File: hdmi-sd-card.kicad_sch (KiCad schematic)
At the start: 76 parts, among them J11 I-PEX_CABLINE-VS_1x20_20455-A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, J4 HDMI-A_WE_685119134923, J5 MicroSD_693071020811, U10 TPD4E05U06QDQARQ1, U11 TPD4E05U06QDQARQ1, U12 TPD4E05U06QDQARQ1, U14 TPD4E05U06QDQARQ1, U37 TPD4E05U06QDQARQ1, U38 SN65DP159RGZR, U40 NVT4858_XQFN, U41 TPD4E05U06QDQARQ1, U43 TPS2116DRLR

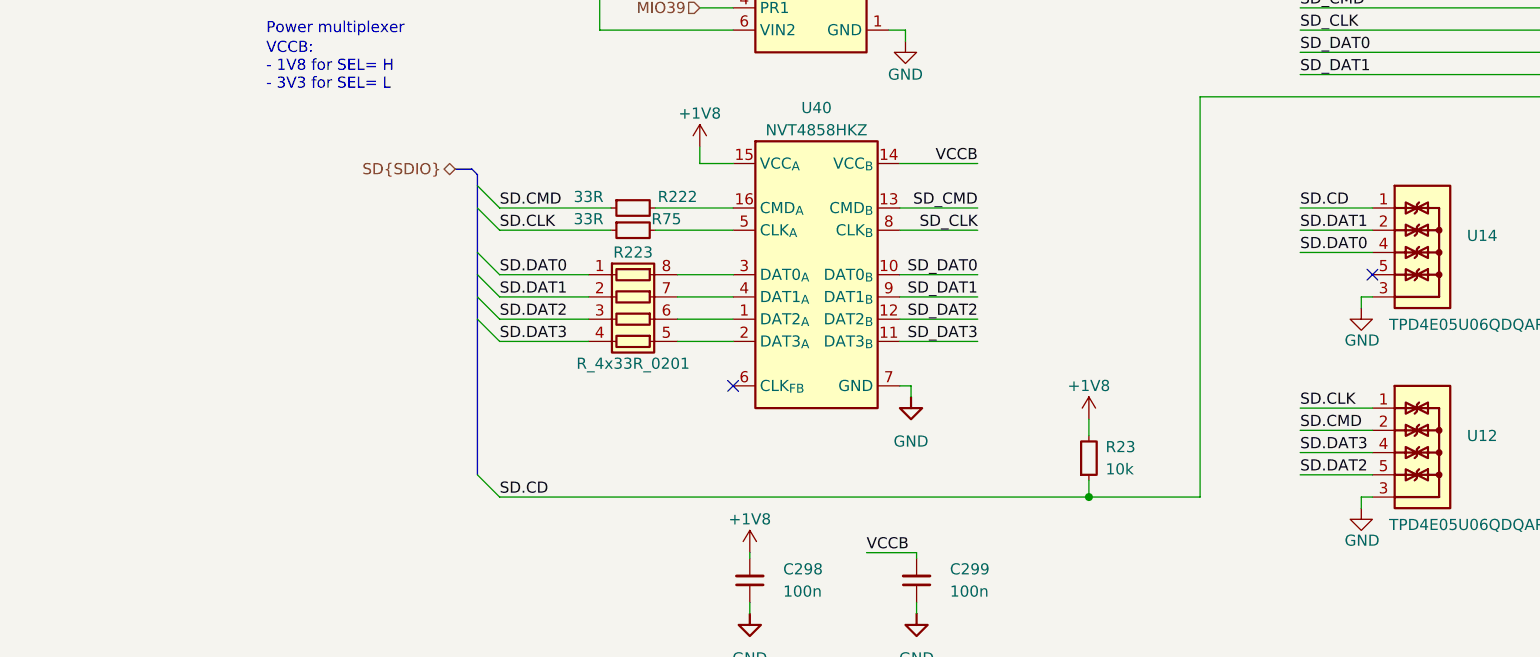
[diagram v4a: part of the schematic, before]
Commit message: [#67016] Connect SD card
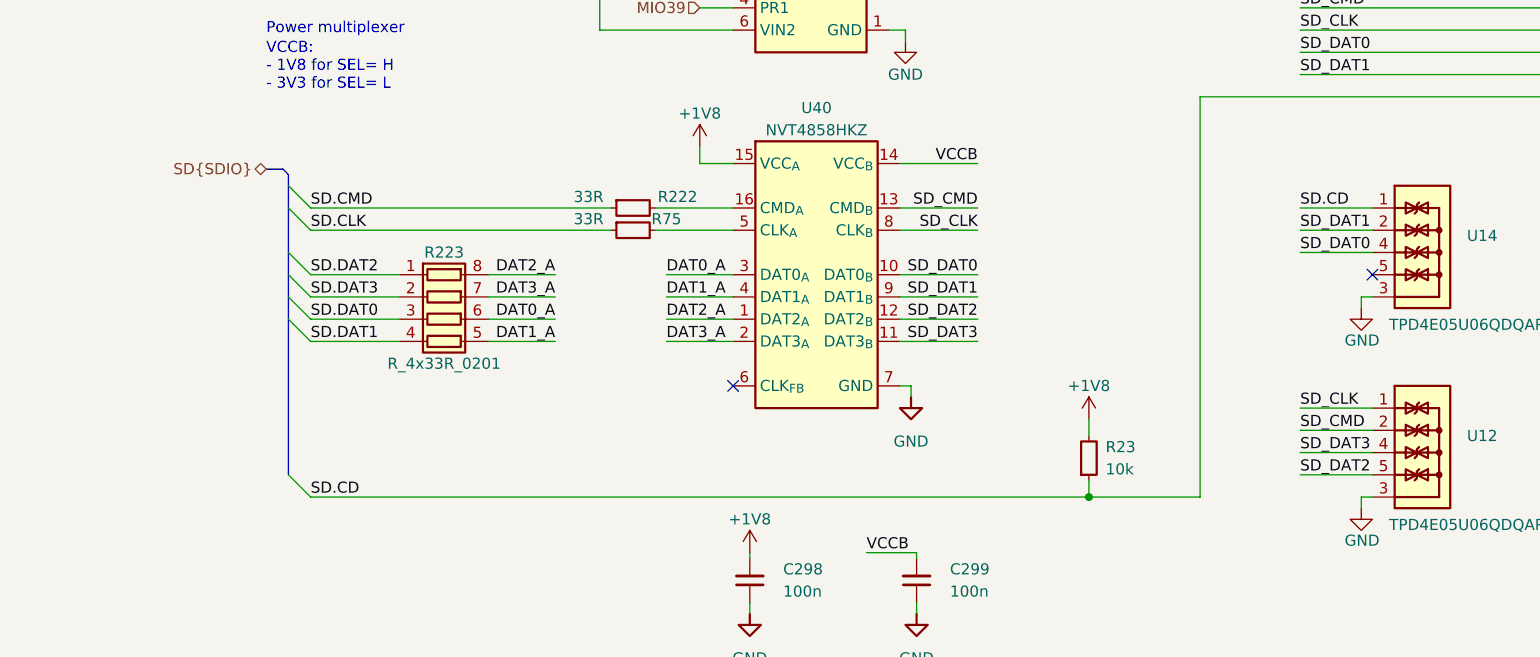
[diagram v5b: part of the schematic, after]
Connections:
- net SD.CLK: no longer U12.1, U12.10
- net SD.CMD: no longer U12.2, U12.9
- net SD.DAT0: now also R223.3 (R3.1); no longer R223.1 (R1.1), U14.4, U14.7
- net SD.DAT1: now also R223.4 (R4.1); no longer R223.2 (R2.1), U14.2, U14.9
- net SD.DAT2: now also R223.1 (R1.1); no longer R223.3 (R3.1), U12.5, U12.6
- net SD.DAT3: now also R223.2 (R2.1); no longer R223.4 (R4.1), U12.4, U12.7
- net SD_CLK: now also U12.1, U12.10
- net SD_CMD: now also U12.2, U12.9
- net SD_DAT0: now also U14.4, U14.7
- net SD_DAT1: now also U14.2, U14.9
- net SD_DAT2: now also U12.5, U12.6
- net SD_DAT3: now also U12.4, U12.7
- net DAT0_A: now reaches R223.6 (R3.2)
- net DAT0_A: now also U40.3 (DAT0_{A}); no longer U40.1 (DAT2_{A})
- net DAT1_A: now reaches R223.5 (R4.2)
- net DAT1_A: now also U40.4 (DAT1_{A}); no longer U40.2 (DAT3_{A})
- net DAT2_A: now reaches R223.8 (R1.2)
- net DAT2_A: now also U40.1 (DAT2_{A}); no longer U40.3 (DAT0_{A})
- net DAT3_A: now reaches R223.7 (R2.2)
- net DAT3_A: now also U40.2 (DAT3_{A}); no longer U40.4 (DAT1_{A})
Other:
- moved on the sheet: R223

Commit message: [#66312] Continued HDMI schematic connections
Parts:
- added C29, C82, C93: C_100n_0402, antmicro-footprints:C_0402_1005Metric, symbol antmicroCapacitors0402:C_100n_0402
- added Q18, Q19, Q21: BSS138PW, antmicro-footprints:SC70-3, symbol antmicroTransistorsFETsMOSFETsSingle:BSS138PW
- added R38: R_0R_0402, antmicro-footprints:R_0402_1005Metric, symbol antmicroResistors0402:R_0R_0402
- added R81, R82: R_1k_0402, antmicro-footprints:R_0402_1005Metric, symbol antmicroResistors0402:R_1k_0402
- added R83: R_100k_0402, antmicro-footprints:R_0402_1005Metric, symbol antmicroResistors0402:R_100k_0402
- added R85, R86: R_10k_0402, antmicro-footprints:R_0402_1005Metric, symbol antmicroResistors0402:R_10k_0402
- added U42: M24C64-F_DFN8, antmicro-footprints:DFN-8-1EP_3x2mm_P0.5mm_EP1.36x1.46mm, symbol antmicroMemory:M24C64-F_DFN8
- added U44: TXS0102DQER, antmicro-footprints:X2SON8_1.4x1x0.32mm_P0.35mm, symbol antmicroLogicTranslatorsLevelShifters:TXS0102DQER
- added U47, U48: TPD4E05U06QDQARQ1, antmicro-footprints:USON-10_2.5x1mm_P0.5mm, symbol antmicroTVSDiodes:TPD4E05U06QDQARQ1
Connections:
- net HDMI_HOTPLUG is gone; now on net I2C_EN/PIN: U38.10 (I2C_EN/PIN)
- net HDMI_IN_CONN_CLK_N is gone; now on net HDMI_IN.CLK_N: U41.5, U41.6
- net HDMI_IN_CONN_CLK_P is gone; now on net HDMI_IN.CLK_P: U41.4, U41.7
- net HDMI_IN_CONN_D0_N is gone; now on net HDMI_IN.D0_N: U41.2, U41.9
- net HDMI_IN_CONN_D0_P is gone; now on net HDMI_IN.D0_P: U41.1, U41.10
- net HDMI_IN_CONN_D1_N is gone; now on net HDMI_IN.D1_N: U37.5, U37.6
- net HDMI_IN_CONN_D1_P is gone; now on net HDMI_IN.D1_P: U37.4, U37.7
- net HDMI_IN_CONN_D2_N is gone; now on net HDMI_IN.D2_N: U37.2, U37.9
- net HDMI_IN_CONN_D2_P is gone; now on net HDMI_IN.D2_P: U37.1, U37.10
- net +3V3: now also C29.1, C82.1, R86.2, U42.8 (VCC), U44.1 (VCCA), U44.5 (OE)
- net +5V: no longer R72.2, R73.2
- net GND: now also C29.2, C82.2, C93.2, Q18.2 (S), Q19.2 (S), Q21.2 (S), R83.1, R85.1, U42.1 (E0), U42.2 (E1), U42.3 (E2), U42.4 (VSS), U42.7 (~{WC}), U42.9 (VSS), U44.4 (GND), U47.3, U47.8, U48.3, U48.8
- net HDMI0.HPD: now also R38.2, U48.4, U48.7; no longer J11.19, U38.33 (HPD_SNK)
- net HDMI0.SCL: now also U48.1, U48.10; no longer J11.15, J4.15 (SCL), R73.1, U38.38 (SCL_SNK)
- net HDMI0.SDA: now also U48.2, U48.9; no longer J11.16, J4.16 (SDA), R72.1, U38.39 (SDA_SNK)
- net HDMI_CONN_5V: now also R72.2, R73.2, U48.5, U48.6
- net HDMI_CTL.SCL: now also U42.6 (SCL)
- net HDMI_CTL.SDA: now also U42.5 (SDA)
- net HDMI_OE: now reaches C294.1, U38.42 (OE)
- net HDMI_IN_5V: now reaches J11.18
- net HDMI_IN_5V: now also C93.1, Q21.1 (G), R81.2, R82.2, R85.2, U44.8 (VCCB), U47.4, U47.7
- net HDMI.SCL renamed HDMI_OUT_I2C.SCL
- net HDMI.SDA renamed HDMI_OUT_I2C.SDA
- new net: R38.1, U38.33 (HPD_SNK)
- new net: Q18.1 (G), Q19.3 (D), R82.1
- new net HDMI_IN_5V.SCL: J11.16, U44.6 (B2), U47.2, U47.9
- new net HDMI_IN_5V.SDA: J11.15, U44.7 (B1), U47.1, U47.10
- new net HDMI_IN_CD: Q21.3 (D), R86.1
- new net HDMI_IN_HPD: J11.19, Q18.3 (D), Q19.1 (G), R81.1, R83.2, U47.5, U47.6
- new net HDMI_IN_I2C.SCL: U44.3 (A2)
- new net HDMI_IN_I2C.SDA: U44.2 (A1)
- new net HDMI_OUT_C.SCL: J4.15 (SCL), R73.1, U38.38 (SCL_SNK)
- new net HDMI_OUT_C.SDA: J4.16 (SDA), R72.1, U38.39 (SDA_SNK)
- new net HDMI_OUT_HPD: U38.10 (I2C_EN/PIN)
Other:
- note added: "HDMI IN"
- note added: "HDMI OUT"
- note removed: "HDMI"
- moved on the sheet: C126, C129, C132, C273, C274, C277, C278, C280, C281, C282, C283, C284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

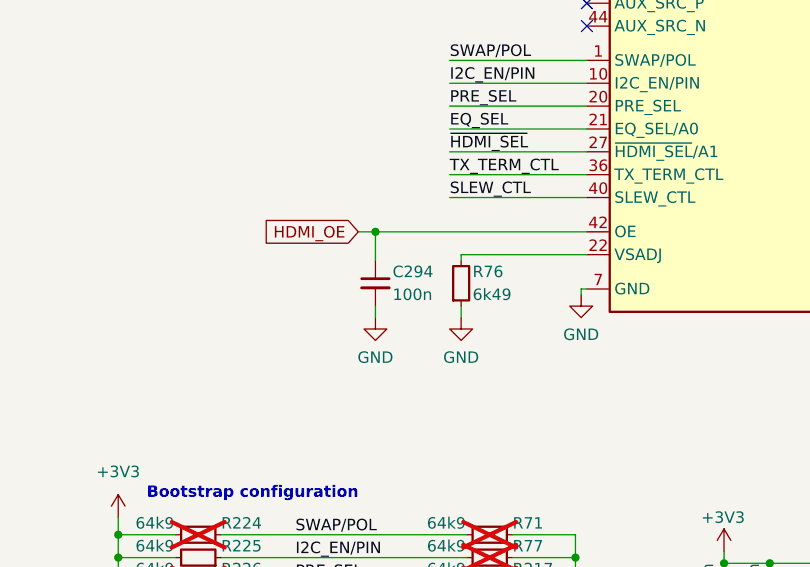
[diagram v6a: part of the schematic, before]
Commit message: [#66312] Connected LS HDMI signals
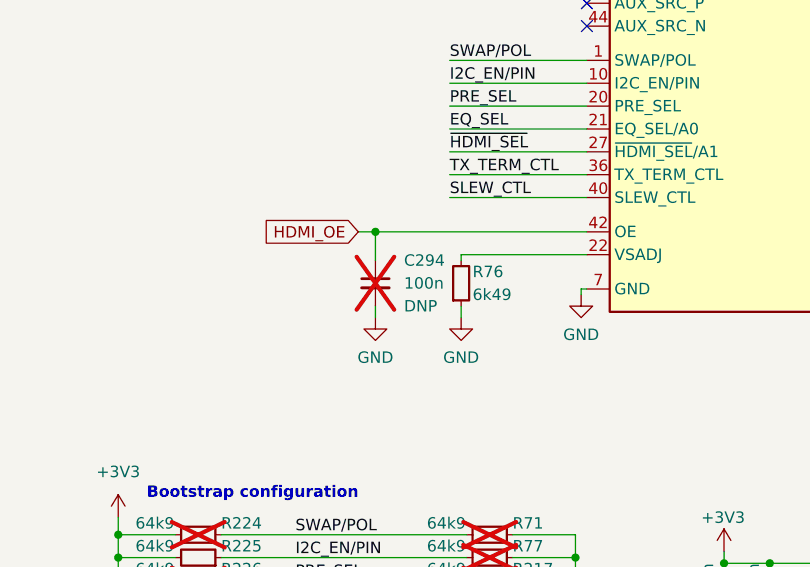
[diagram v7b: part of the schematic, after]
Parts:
- C294: DNP (none) -> DNP; now not fitted
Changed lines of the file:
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@@
   )
   (symbol (lib_id "antmicroCapacitors0402:C_100n_0402") (at 53.975 227.965 270) (unit 1)
-    (in_bom yes) (on_board yes) (dnp no)
-    (property "Reference" "C294" (at 55.88 229.235 90)
+    (in_bom yes) (on_board yes) (dnp yes) (fields_autoplaced)
+    (property "Reference" "C294" (at 57.15 227.9713 90)
       (effects (font (size 1.27 1.27) (thickness 0.15)) (justify left))
     )
@@
       (effects (font (size 1.27 1.27) (thickness 0.15)) (justify left bottom) hide)
     )
-    (property "Val" "100n" (at 55.88 231.775 90)
+    (property "Val" "100n" (at 57.15 230.5113 90)
       (effects (font (size 1.27 1.27) (thickness 0.15)) (justify left))
     )
@@
       (effects (font (size 1.27 1.27)) (justify left bottom) hide)
     )
+    (property "DNP" "DNP" (at 57.15 233.0513 90)
+      (effects (font (size 1.27 1.27)) (justify left))
+    )
     (pin "2")

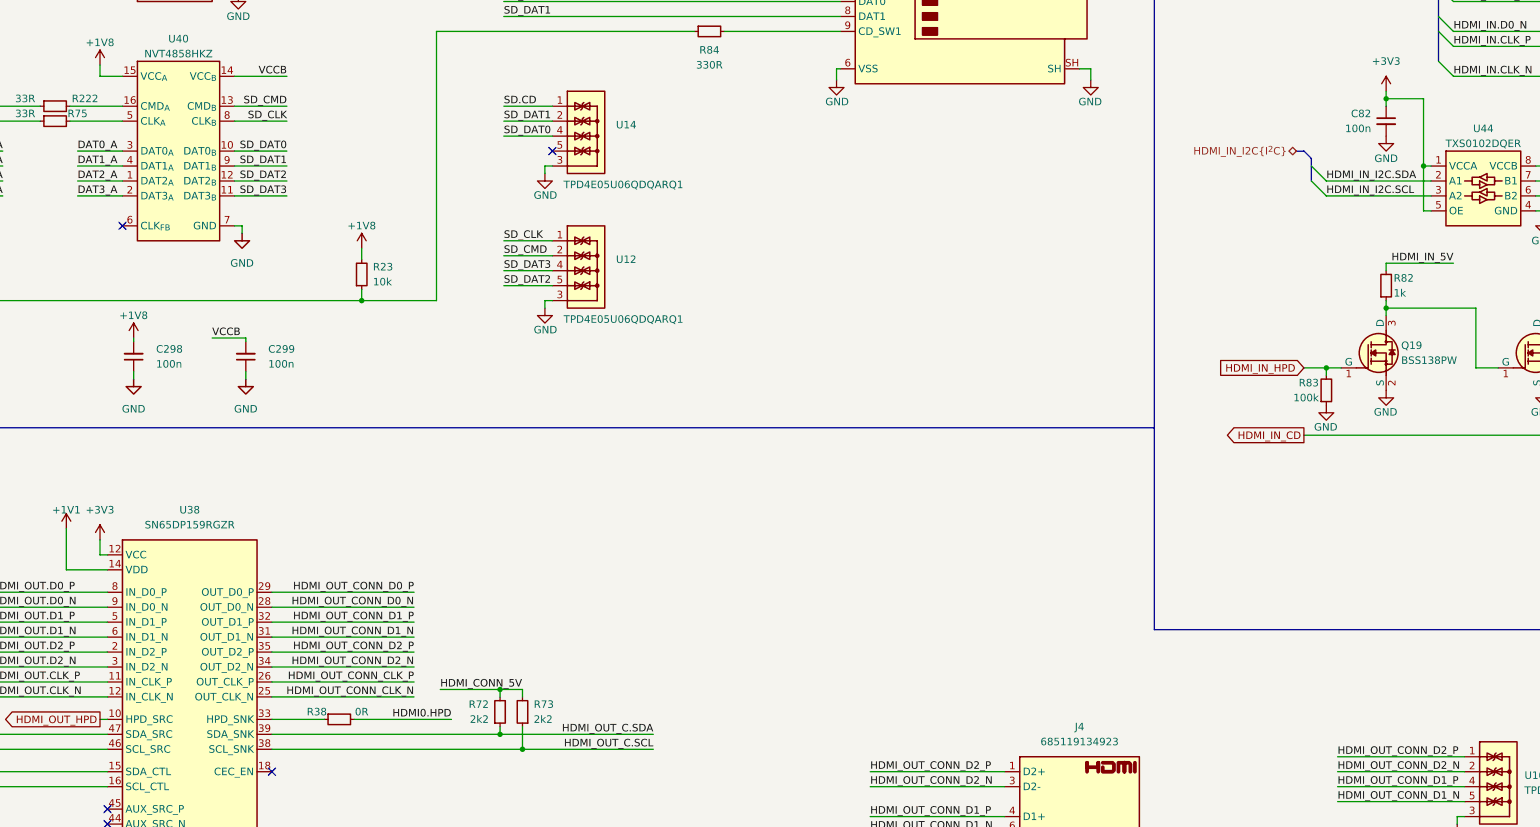
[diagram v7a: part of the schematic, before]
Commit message: [#66727] Fix schematic errors
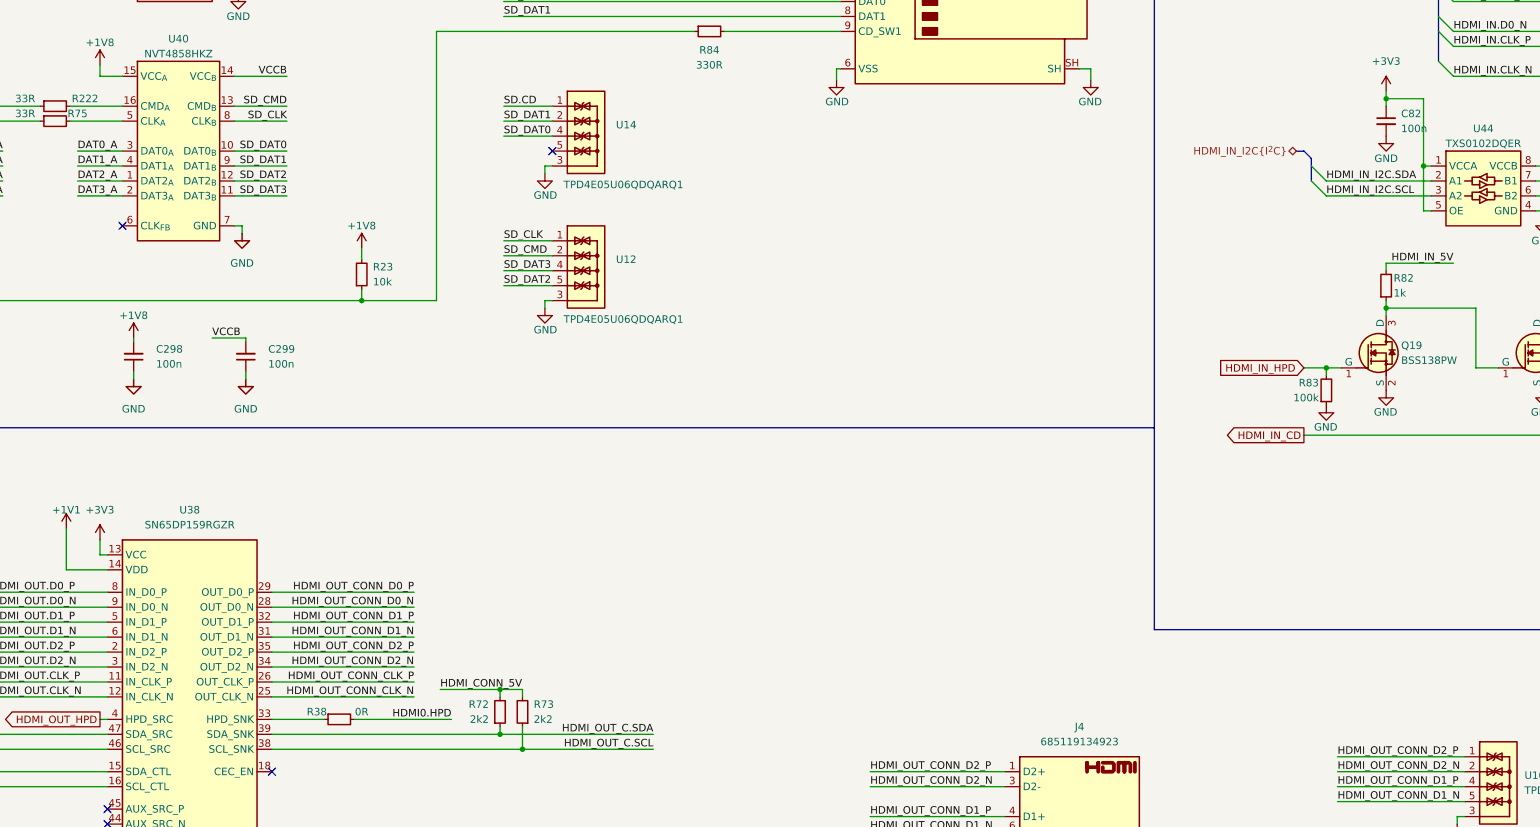
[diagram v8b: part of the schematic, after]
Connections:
- net +3V3: now also U38.13 (VCC); no longer U38.12 (VCC)
- net HDMI_OUT_HPD: now also U38.4 (HPD_SRC); no longer U38.10 (I2C_EN/PIN)
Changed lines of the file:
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@@
     (pin "33")
     (pin "18")
-    (pin "12")
+    (pin "13")
     (pin "15")
     (pin "10")
@@
     (pin "17")
     (pin "16")
-    (pin "10")
+    (pin "4")
     (instances
       (project "data-center-rdimm-ddr5-tester"
@@
   (symbol (lib_id "antmicroCapacitors0402:C_100n_0402") (at 294.64 80.01 270) (unit 1)
     (in_bom yes) (on_board yes) (dnp no) (fields_autoplaced)
-    (property "Reference" "C82" (at 292.1 81.2863 90)
-      (effects (font (size 1.27 1.27) (thickness 0.15)) (justify right))
+    (property "Reference" "C82" (at 297.18 81.2863 90)
+      (effects (font (size 1.27 1.27) (thickness 0.15)) (justify left))
     )
     (property "Value" "C_100n_0402" (at 284.48 100.33 0)
@@
       (effects (font (size 1.27 1.27) (thickness 0.15)) (justify left bottom) hide)
     )
-    (property "Val" "100n" (at 292.1 83.8263 90)
-      (effects (font (size 1.27 1.27) (thickness 0.15)) (justify right))
+    (property "Val" "100n" (at 297.18 83.8263 90)
+      (effects (font (size 1.27 1.27) (thickness 0.15)) (justify left))
     )
     (property "Voltage" "50V" (at 266.7 100.33 0)
